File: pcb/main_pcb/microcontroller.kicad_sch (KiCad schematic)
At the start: 23 parts, among them J1 Conn_01x05, J10 Conn_01x06_Male, J2 Conn_01x05, J3 Conn_01x05, J4 Conn_01x05, J5 Conn_01x05, J6 Conn_01x05, J7 Conn_01x04, J8 Conn_01x06_Male, U3 DRV8833

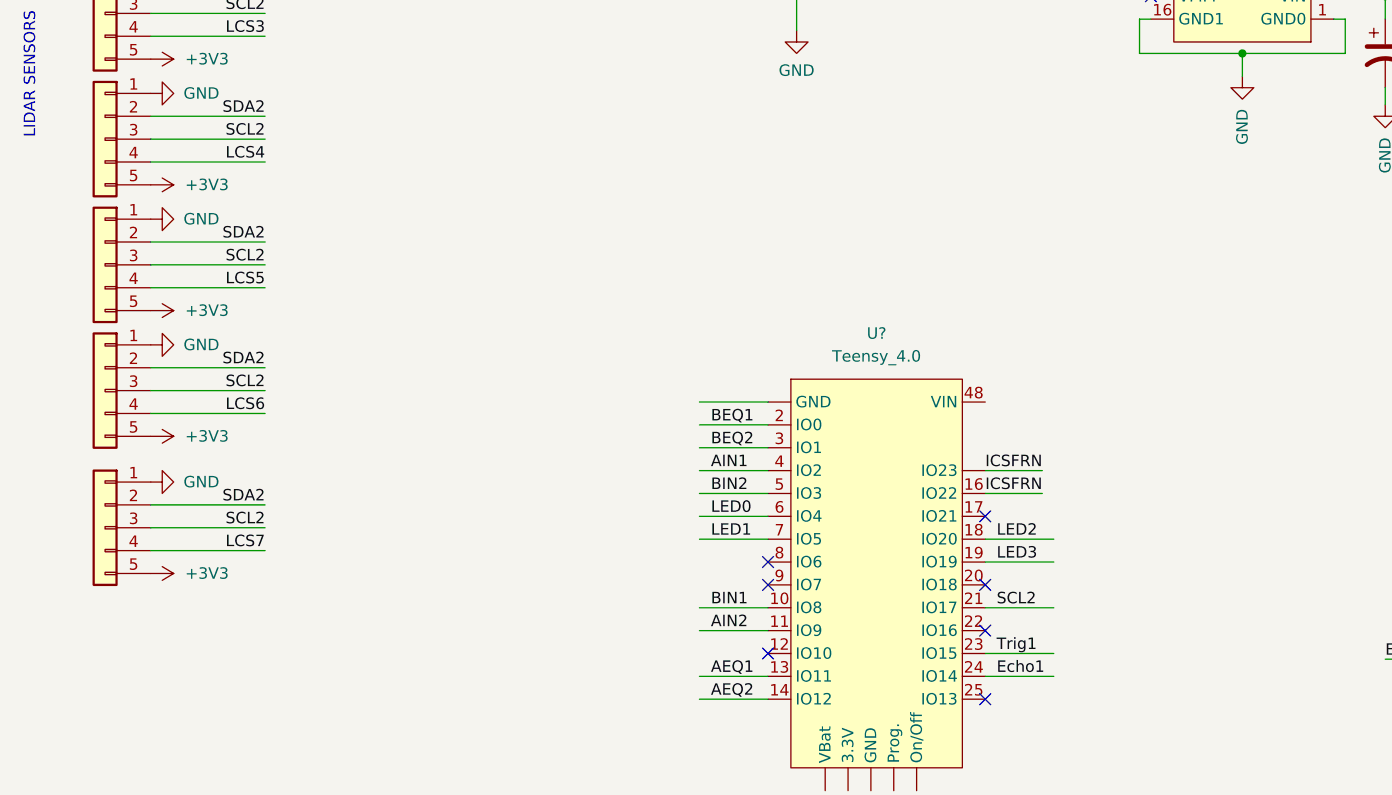
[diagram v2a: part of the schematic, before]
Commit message: Adding LCS branches
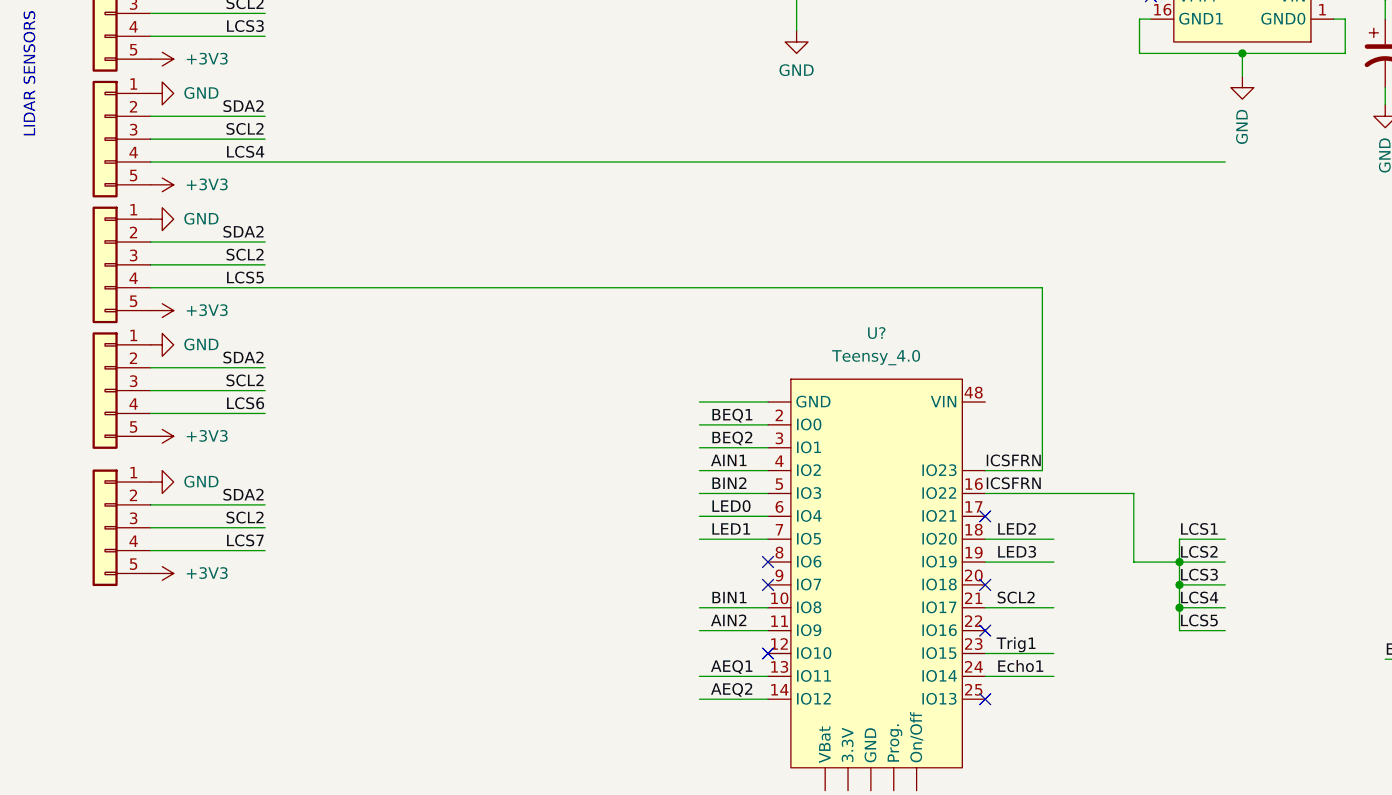
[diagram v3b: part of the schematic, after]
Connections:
- net LCS1 is gone; now on net ICSFRN: J1.4 (Pin_4)
- net LCS2 is gone; now on net ICSFRN: J2.4 (Pin_4)
- net LCS3 is gone; now on net ICSFRN: J3.4 (Pin_4)
- net LCS4 is gone; now on net ICSFRN: J4.4 (Pin_4)
- net LCS5 is gone; now on net ICSFRN: J5.4 (Pin_4)
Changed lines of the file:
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@@
   (junction (at 172.72 62.865) (diameter 0) (color 0 0 0 0)
   )
+  (junction (at 149.86 128.27) (diameter 0) (color 0 0 0 0)
+  )
+  (junction (at 149.86 130.81) (diameter 0) (color 0 0 0 0)
+  )
   (junction (at 182.88 136.525) (diameter 0) (color 0 0 0 0)
   )
@@
   )
   (junction (at 107.315 51.435) (diameter 0) (color 0 0 0 0)
+  )
+  (junction (at 149.86 125.73) (diameter 0) (color 0 0 0 0)
   )
   (junction (at 107.315 59.055) (diameter 0) (color 0 0 0 0)
@@
   (no_connect (at 146.685 47.625))
   (no_connect (at 104.14 128.27))
-  (no_connect (at 104.14 135.89))
   (no_connect (at 128.27 120.65))
   (no_connect (at 128.27 140.97))
+  (no_connect (at 104.14 135.89))
   (wire (pts (xy 35.56 39.37) (xy 48.26 39.37))
     (stroke (width 0) (type default) (color 0 0 0 0))
@@
     (stroke (width 0) (type default) (color 0 0 0 0))
   )
+  (wire (pts (xy 149.86 130.81) (xy 149.86 133.35))
+    (stroke (width 0) (type default) (color 0 0 0 0))
+  )
   (wire (pts (xy 35.56 78.74) (xy 48.26 78.74))
     (stroke (width 0) (type default) (color 0 0 0 0))
@@
     (stroke (width 0) (type default) (color 0 0 0 0))
   )
+  (wire (pts (xy 144.78 118.11) (xy 144.78 125.73))
+    (stroke (width 0) (type default) (color 0 0 0 0))
+  )
   (wire (pts (xy 96.52 133.35) (xy 104.14 133.35))
     (stroke (width 0) (type default) (color 0 0 0 0))
@@
     (stroke (width 0) (type default) (color 0 0 0 0))
   )
+  (wire (pts (xy 128.27 118.11) (xy 144.78 118.11))
+    (stroke (width 0) (type default) (color 0 0 0 0))
+  )
   (wire (pts (xy 128.27 123.19) (xy 135.89 123.19))
     (stroke (width 0) (type default) (color 0 0 0 0))
   )
+  (wire (pts (xy 144.78 125.73) (xy 149.86 125.73))
+    (stroke (width 0) (type default) (color 0 0 0 0))
+  )
   (wire (pts (xy 247.65 62.865) (xy 243.84 62.865))
     (stroke (width 0) (type default) (color 0 0 0 0))
@@
     (stroke (width 0) (type default) (color 0 0 0 0))
   )
+  (wire (pts (xy 149.86 125.73) (xy 154.94 125.73))
+    (stroke (width 0) (type default) (color 0 0 0 0))
+  )
   (wire (pts (xy 35.56 67.31) (xy 48.26 67.31))
     (stroke (width 0) (type default) (color 0 0 0 0))
@@
     (stroke (width 0) (type default) (color 0 0 0 0))
   )
+  (wire (pts (xy 149.86 125.73) (xy 149.86 128.27))
+    (stroke (width 0) (type default) (color 0 0 0 0))
+  )
   (wire (pts (xy 35.56 76.2) (xy 48.26 76.2))
     (stroke (width 0) (type default) (color 0 0 0 0))
@@
     (stroke (width 0) (type default) (color 0 0 0 0))
   )
-  (wire (pts (xy 35.56 95.25) (xy 48.26 95.25))
+  (wire (pts (xy 149.86 128.27) (xy 149.86 130.81))
     (stroke (width 0) (type default) (color 0 0 0 0))
   )
@@
     (stroke (width 0) (type default) (color 0 0 0 0))
   )
+  (wire (pts (xy 35.56 95.25) (xy 134.62 95.25))
+    (stroke (width 0) (type default) (color 0 0 0 0))
+  )
   (wire (pts (xy 234.95 60.325) (xy 247.65 60.325))
     (stroke (width 0) (type default) (color 0 0 0 0))
@@
     (stroke (width 0) (type default) (color 0 0 0 0))
   )
+  (wire (pts (xy 35.56 81.28) (xy 154.94 81.28))
+    (stroke (width 0) (type default) (color 0 0 0 0))
+  )
   (wire (pts (xy 107.315 36.195) (xy 107.315 43.815))
     (stroke (width 0) (type default) (color 0 0 0 0))
@@
     (stroke (width 0) (type default) (color 0 0 0 0))
   )
-  (wire (pts (xy 128.27 118.11) (xy 134.62 118.11))
-    (stroke (width 0) (type default) (color 0 0 0 0))
-  )
   (wire (pts (xy 156.845 69.215) (xy 156.845 71.755))
     (stroke (width 0) (type default) (color 0 0 0 0))
@@
     (stroke (width 0) (type default) (color 0 0 0 0))
   )
+  (wire (pts (xy 149.86 128.27) (xy 154.94 128.27))
+    (stroke (width 0) (type default) (color 0 0 0 0))
+  )
   (wire (pts (xy 202.565 45.085) (xy 202.565 55.245))
     (stroke (width 0) (type default) (color 0 0 0 0))
@@
     (stroke (width 0) (type default) (color 0 0 0 0))
   )
+  (wire (pts (xy 149.86 133.35) (xy 154.94 133.35))
+    (stroke (width 0) (type default) (color 0 0 0 0))
+  )
+  (wire (pts (xy 149.86 130.81) (xy 154.94 130.81))
+    (stroke (width 0) (type default) (color 0 0 0 0))
+  )
   (wire (pts (xy 35.56 109.22) (xy 48.26 109.22))
     (stroke (width 0) (type default) (color 0 0 0 0))
   )
+  (wire (pts (xy 134.62 95.25) (xy 134.62 115.57))
+    (stroke (width 0) (type default) (color 0 0 0 0))
+  )
   (wire (pts (xy 96.52 138.43) (xy 104.14 138.43))
     (stroke (width 0) (type default) (color 0 0 0 0))
   )
+  (wire (pts (xy 149.86 125.73) (xy 149.86 123.19))
+    (stroke (width 0) (type default) (color 0 0 0 0))
+  )
   (wire (pts (xy 172.72 136.525) (xy 182.88 136.525))
     (stroke (width 0) (type default) (color 0 0 0 0))
@@
     (stroke (width 0) (type default) (color 0 0 0 0))
   )
-  (wire (pts (xy 35.56 81.28) (xy 48.26 81.28))
-    (stroke (width 0) (type default) (color 0 0 0 0))
-  )
   (wire (pts (xy 35.56 48.26) (xy 48.26 48.26))
     (stroke (width 0) (type default) (color 0 0 0 0))
@@
   )
   (wire (pts (xy 191.135 60.325) (xy 203.835 60.325))
+    (stroke (width 0) (type default) (color 0 0 0 0))
+  )
+  (wire (pts (xy 149.86 123.19) (xy 154.94 123.19))
     (stroke (width 0) (type default) (color 0 0 0 0))
   )
@@
     (effects (font (size 1.27 1.27)) (justify right bottom))
   )
+  (label "LCS4" (at 149.86 130.81 0)
+    (effects (font (size 1.27 1.27)) (justify left bottom))
+  )
   (label "SCL2" (at 48.26 78.74 180)
     (effects (font (size 1.27 1.27)) (justify right bottom))
@@
     (effects (font (size 1.27 1.27)) (justify left bottom))
   )
+  (label "LCS2" (at 149.86 125.73 0)
+    (effects (font (size 1.27 1.27)) (justify left bottom))
+  )
   (label "SCL2" (at 48.26 50.8 180)
     (effects (font (size 1.27 1.27)) (justify right bottom))
@@
     (effects (font (size 1.27 1.27)) (justify left bottom))
   )
+  (label "LCS3" (at 149.86 128.27 0)
+    (effects (font (size 1.27 1.27)) (justify left bottom))
+  )
   (label "Trig1" (at 129.54 135.89 0)
     (effects (font (size 1.27 1.27)) (justify left bottom))
@@
     (effects (font (size 1.27 1.27)) (justify left bottom))
   )
+  (label "LCS1" (at 149.86 123.19 0)
+    (effects (font (size 1.27 1.27)) (justify left bottom))
+  )
   (label "LED0" (at 73.025 36.195 0)
     (effects (font (size 1.27 1.27)) (justify left bottom))
@@
     (effects (font (size 1.27 1.27)) (justify left bottom))
   )
+  (label "LCS5" (at 149.86 133.35 0)
+    (effects (font (size 1.27 1.27)) (justify left bottom))
+  )

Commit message: Finishing LCS wires
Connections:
- net LCS6 is gone; now on net ICSFRN: J6.4 (Pin_4)
- net LCS7 is gone; now on net ICSFRN: J?.4 (Pin_4)
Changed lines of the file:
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@@
   (junction (at 149.86 130.81) (diameter 0) (color 0 0 0 0)
   )
+  (junction (at 149.86 133.35) (diameter 0) (color 0 0 0 0)
+  )
   (junction (at 182.88 136.525) (diameter 0) (color 0 0 0 0)
   )
@@
   )
   (junction (at 156.845 69.215) (diameter 0) (color 0 0 0 0)
+  )
+  (junction (at 149.86 135.89) (diameter 0) (color 0 0 0 0)
   )
   (junction (at 107.315 51.435) (diameter 0) (color 0 0 0 0)
@@
     (stroke (width 0) (type default) (color 0 0 0 0))
   )
+  (wire (pts (xy 35.56 95.25) (xy 48.26 95.25))
+    (stroke (width 0) (type default) (color 0 0 0 0))
+  )
   (wire (pts (xy 96.52 118.11) (xy 104.14 118.11))
     (stroke (width 0) (type default) (color 0 0 0 0))
@@
     (stroke (width 0) (type default) (color 0 0 0 0))
   )
+  (wire (pts (xy 149.86 135.89) (xy 149.86 138.43))
+    (stroke (width 0) (type default) (color 0 0 0 0))
+  )
   (wire (pts (xy 149.86 128.27) (xy 149.86 130.81))
     (stroke (width 0) (type default) (color 0 0 0 0))
@@
     (stroke (width 0) (type default) (color 0 0 0 0))
   )
-  (wire (pts (xy 35.56 95.25) (xy 134.62 95.25))
-    (stroke (width 0) (type default) (color 0 0 0 0))
-  )
   (wire (pts (xy 234.95 60.325) (xy 247.65 60.325))
     (stroke (width 0) (type default) (color 0 0 0 0))
@@
     (stroke (width 0) (type default) (color 0 0 0 0))
   )
+  (wire (pts (xy 149.86 138.43) (xy 154.94 138.43))
+    (stroke (width 0) (type default) (color 0 0 0 0))
+  )
   (wire (pts (xy 35.56 121.92) (xy 48.26 121.92))
     (stroke (width 0) (type default) (color 0 0 0 0))
@@
     (stroke (width 0) (type default) (color 0 0 0 0))
   )
+  (wire (pts (xy 149.86 135.89) (xy 154.94 135.89))
+    (stroke (width 0) (type default) (color 0 0 0 0))
+  )
   (wire (pts (xy 149.86 130.81) (xy 154.94 130.81))
     (stroke (width 0) (type default) (color 0 0 0 0))
@@
     (stroke (width 0) (type default) (color 0 0 0 0))
   )
-  (wire (pts (xy 134.62 95.25) (xy 134.62 115.57))
-    (stroke (width 0) (type default) (color 0 0 0 0))
-  )
   (wire (pts (xy 96.52 138.43) (xy 104.14 138.43))
+    (stroke (width 0) (type default) (color 0 0 0 0))
+  )
+  (wire (pts (xy 149.86 133.35) (xy 149.86 135.89))
     (stroke (width 0) (type default) (color 0 0 0 0))
   )
@@
     (effects (font (size 1.27 1.27)) (justify right bottom))
   )
+  (label "LCS7" (at 149.86 138.43 0)
+    (effects (font (size 1.27 1.27)) (justify left bottom))
+  )
   (label "SCL2" (at 48.26 106.68 180)
     (effects (font (size 1.27 1.27)) (justify right bottom))
@@
     (effects (font (size 1.27 1.27)) (justify left bottom))
   )
+  (label "LCS6" (at 149.86 135.89 0)
+    (effects (font (size 1.27 1.27)) (justify left bottom))
+  )
